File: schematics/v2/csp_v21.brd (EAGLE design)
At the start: 100 x 67 mm, 65 parts, among them IC1 74AHC1G08DCK, IC2 74HCT04D, IC3 PCA9555PW, IC4 LM339D, J1 2X20-CHIP2X20-SMT-CHIP, Q1 BSS84, Q2 BSS123, U2 DS2431P

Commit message: added v2.1, with 5V switchable to avoid discharge
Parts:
- moved SJ3 24.0 mm to (69.5, 40.9), flipped to the top, turned to 180 degrees
- moved G 22.8 mm to (35.2, 53.8)
- moved U$5 1.90 mm to (66.0, 40.1)
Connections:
- net VCC3V3: now also C2.1, C4.1, L2.P$2
- net VCC5V: no longer C2.1, C4.1, L2.P$2
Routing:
- net VCC5V: track 156.8 -> 67.9 mm, vias 6 -> 5
- net VCC3V3: track 293.4 -> 328.8 mm, vias 20 -> 17
- net VCC3V3_2: track 2.14 -> 13.6 mm, vias 0 -> 1
- net GND: vias 29 -> 30

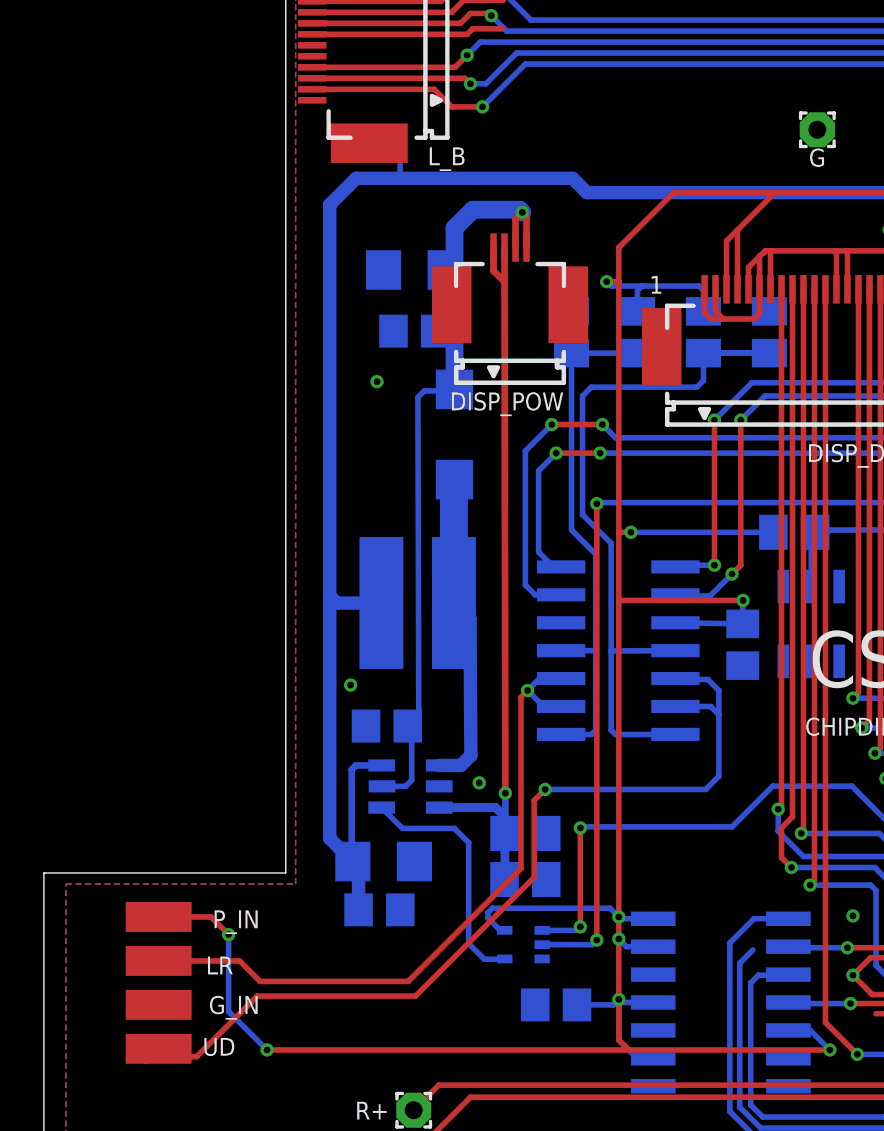
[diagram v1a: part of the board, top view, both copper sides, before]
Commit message: Fixed Op-amp, position of thumb still wrong
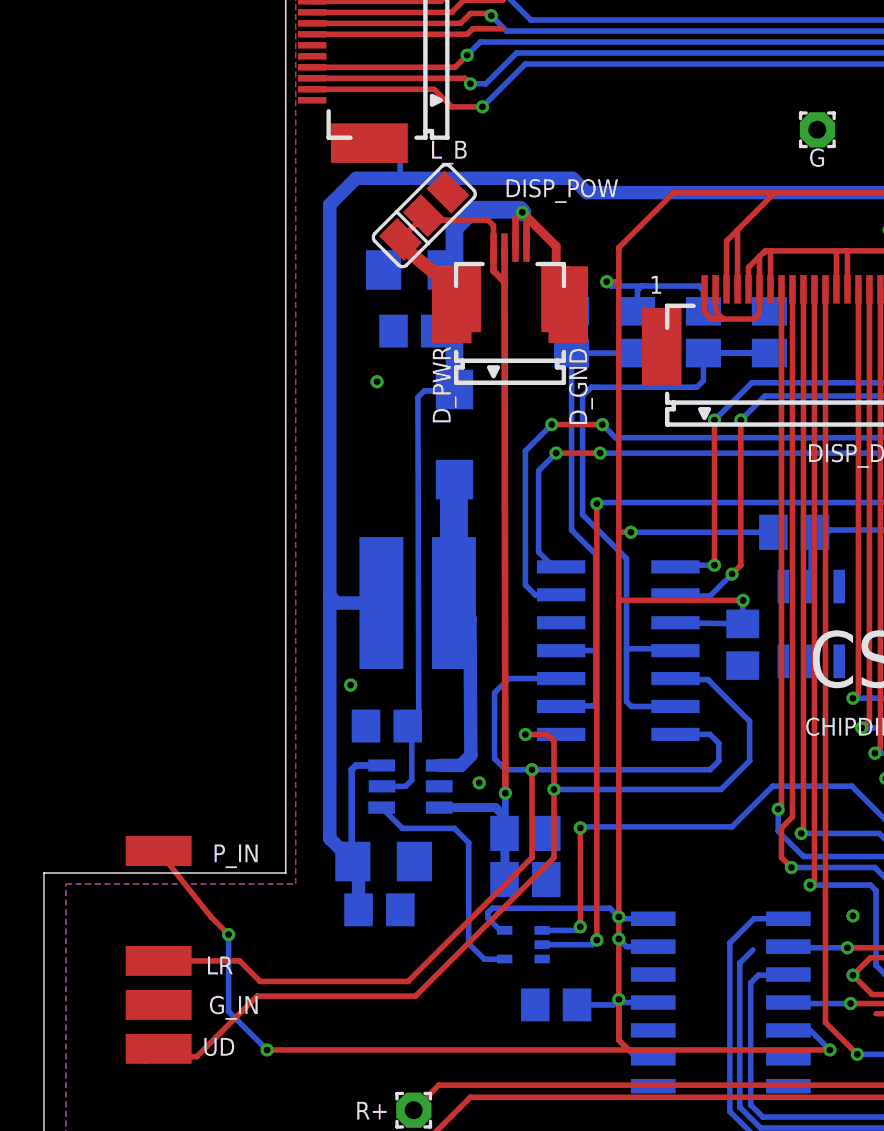
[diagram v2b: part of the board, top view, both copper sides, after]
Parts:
- added D_GND: D_GND, JKW_CHIP:SMD1,36-3
- added D_PWR: D_PWR, JKW_CHIP:SMD1,36-3
- added U$28: SMD_SJ_3WAY_CLOSED, JKW_CHIP:SMD_SJ_3WAY_CLOSED
- moved P_IN 3.00 mm to (5.22, 21.0)
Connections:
- new net N$28: D_PWR.P$1, U$28.1
- net 1V: now also IC4.6; no longer IC4.7
- net 2V: now also IC4.9; no longer IC4.8
- net DISPL_GND: now also U$28.2
- net FB: now also D_GND.P$1
- net N$30: now also IC4.8; no longer IC4.6
- net N$31: now also IC4.7; no longer IC4.9
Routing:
- net N$31: track 30.8 -> 43.5 mm
- net FB: track 36.7 -> 41.3 mm
- net N$30: track 42.2 -> 46.7 mm, vias 1 -> 2
- net DISPL_GND: track 34.9 -> 39.3 mm
- net N$28: track 0.00 -> 4.12 mm
- net 1V: track 34.7 -> 32.4 mm
- net VCC3V3: track 328.8 -> 330.2 mm
- net 2V: track 23.8 -> 22.6 mm

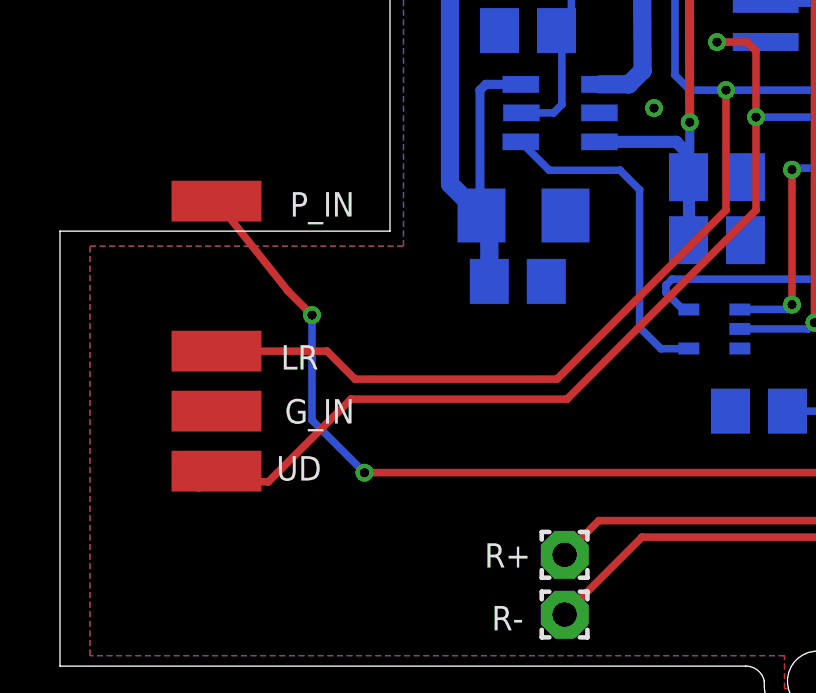
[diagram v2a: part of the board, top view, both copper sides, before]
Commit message: moved pads for analog input
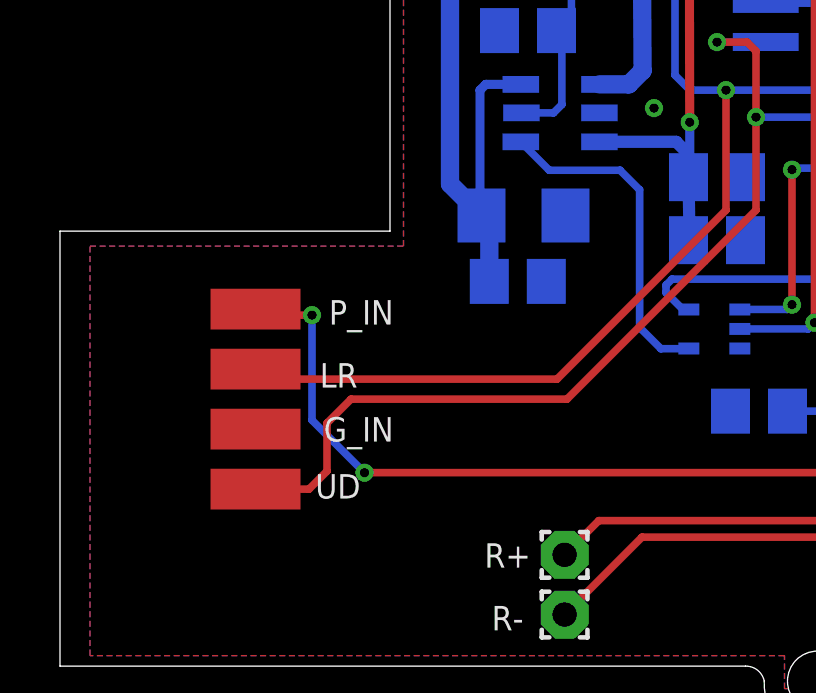
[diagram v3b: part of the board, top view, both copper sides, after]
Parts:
- moved P_IN 3.83 mm to (6.52, 17.4)
- moved G_IN 1.43 mm to (6.52, 13.4)
- moved LR 1.43 mm to (6.52, 15.4)
- moved UD 1.43 mm to (6.52, 11.4)
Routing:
- net VCC3V3: track 330.2 -> 327.2 mm
- net N$31: track 43.5 -> 42.0 mm
- net N$30: track 46.7 -> 45.2 mm
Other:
- board text added: "v3 JKW"
- board text removed: "v2 JKW"
